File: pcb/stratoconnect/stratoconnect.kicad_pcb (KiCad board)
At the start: 2 copper layers, 61.8 x 40 mm, 37 parts, among them J1 Conn_Coaxial, J2 Conn_02x03_Odd_Even, J3 Conn_01x05_Male, J4 Conn_01x02_Male, J5 Conn_01x03_Male, SW1 SW_SPST, SW2 SW_SPST, U1 RF4463f30, U2 ATmega328PB-A, U3 TPS61022RWU, Y1 CSTNE16M0V530000R0

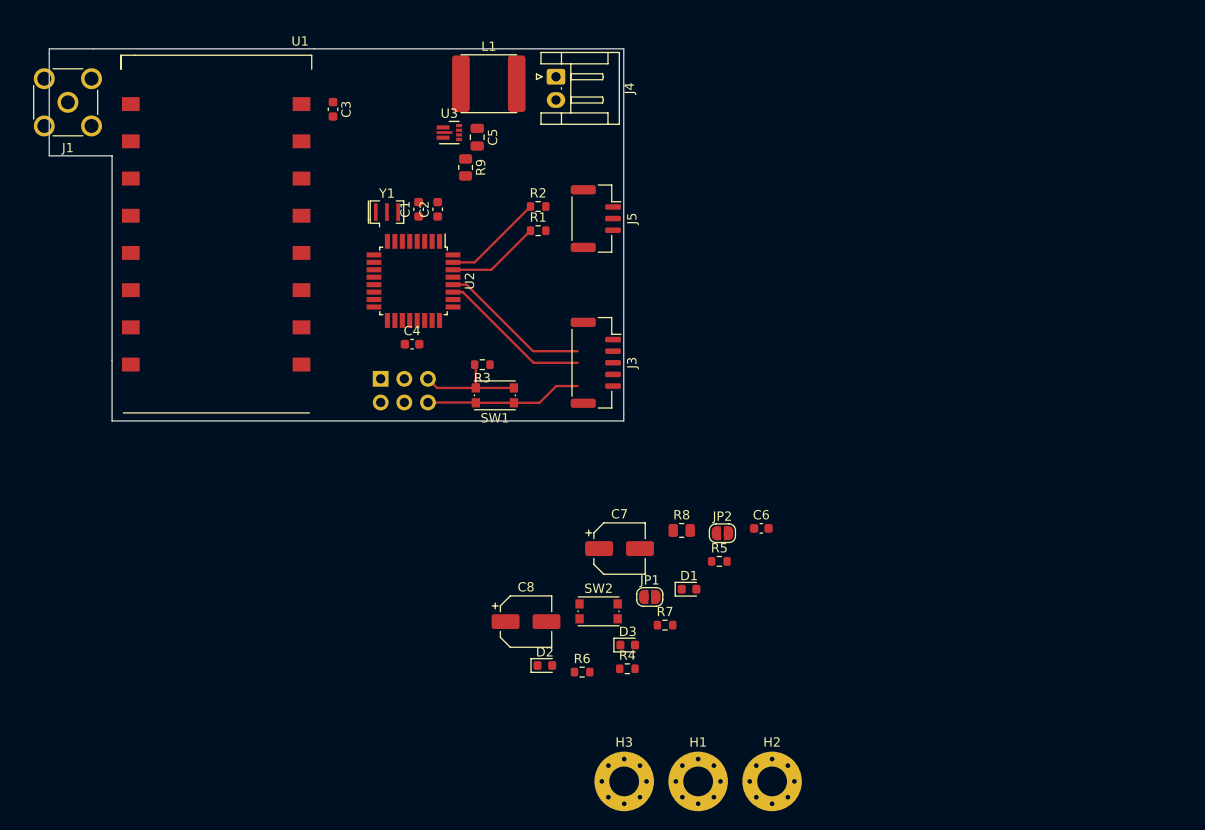
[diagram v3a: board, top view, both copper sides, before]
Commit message: finish routing the smps, need to extend the footprint pads for the rf module
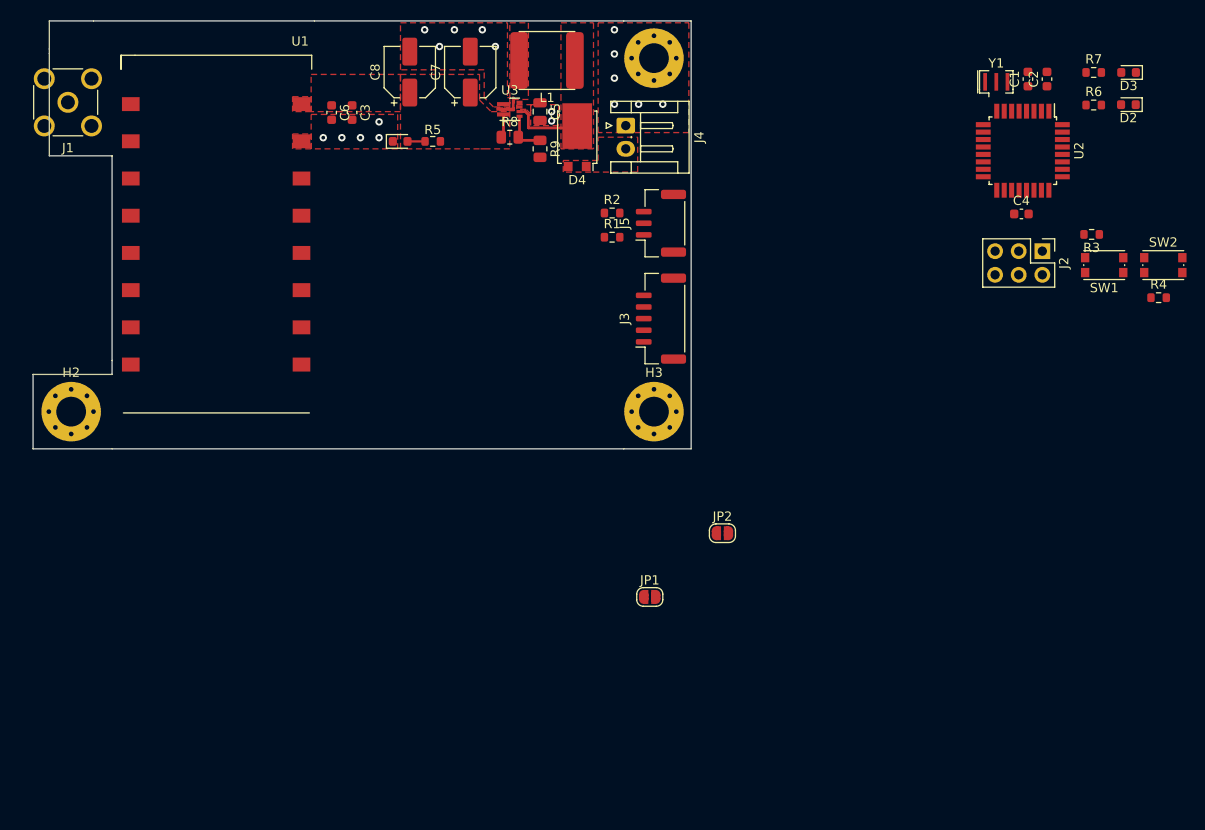
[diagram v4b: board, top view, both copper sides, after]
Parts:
- added D4: ST12199STR, Kevin_Lutzer_Lbr:Diode-TO-277B, F.Cu at (196.0, 59.8)
- J2: moved to F.Cu
- moved D2 87.0 mm to (255.2, 56.2), turned to 180 degrees
- moved H2 85.2 mm to (141.6, 89.2)
- moved R6 82.1 mm to (251.5, 56.3)
- moved D3 81.8 mm to (255.3, 52.8), turned to 180 degrees
- moved H1 77.9 mm to (204.2, 51.2)
- moved R7 75.2 mm to (251.5, 52.8)
- moved J2 72.4 mm to (246.0, 72.0)
- moved SW2 71.2 mm to (259.0, 73.5)
- moved R4 69.7 mm to (258.5, 77.0)
- moved C1 67.0 mm to (244.4, 53.5)
- moved C2 67.0 mm to (246.5, 53.5)
- moved C4 67.0 mm to (243.8, 68.0)
- moved R3 67.0 mm to (251.3, 70.2)
- moved SW1 67.0 mm to (252.7, 73.5)
- moved U2 67.0 mm to (243.9, 61.2)
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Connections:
- C5 pad 1: VDC -> /VDC_FWD
- J4 pad 1: +5V -> GND
- J4 pad 2: GND -> VDC
- L1 pad 1: VDC -> /VDC_FWD
- U3 pad 1: Net-(R8-Pad2) -> +5V
- U3 pad 2: VDC -> /SW
- U3 pad 6: Net-(L1-Pad2) -> /VDC_FWD
- U3 pad 7: +5V -> Net-(R8-Pad2)
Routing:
- net GND: track 16.9 -> 0.00 mm, vias 0 -> 18
- net /SDA: track 16.5 -> 0.00 mm
- net /SCL: track 16.4 -> 0.00 mm
- net /~{RST}: track 12.2 -> 0.00 mm
- net Net-(R2-Pad1): track 10.8 -> 0.00 mm
- net Net-(R1-Pad1): track 10.1 -> 0.00 mm
- net /VDC_FWD: track 0.00 -> 7.84 mm
- net Net-(R8-Pad2): track 0.00 -> 4.78 mm
- net +5V: track 0.00 -> 2.55 mm
- net /SW: track 0.00 -> 2.07 mm
- net Net-(D1-Pad2): track 0.00 -> 1.89 mm
- added copper zone on F.Cu, net +5V
- added copper zone on F.Cu, net /SW
- added copper zone on F.Cu, net /VDC_FWD
- added copper zone on F.Cu, net GND
- added copper zone on F.Cu, net VDC
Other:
- board size 61.8 x 40 mm -> 70.8 x 46 mm
- board text added: "Routed on 0,01mm Placed on 0.25mm"

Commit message: WIP
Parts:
- added R10: 22k, Resistor_SMD:R_0603_1608Metric, F.Cu at (242.2, 85.2)
- added R11: 22k, Resistor_SMD:R_0603_1608Metric, F.Cu at (246.2, 85.2)
- moved C2 65.8 mm to (182.1, 66.9)
- moved C4 65.8 mm to (179.3, 81.4)
- moved D2 65.8 mm to (190.8, 69.7)
- moved D3 65.8 mm to (190.9, 66.2)
- moved J2 65.8 mm to (181.6, 85.4)
- moved R3 65.8 mm to (186.9, 83.6)
- moved R4 65.8 mm to (194.1, 90.4)
- moved R6 65.8 mm to (187.1, 69.7)
- moved R7 65.8 mm to (187.1, 66.2)
- moved SW1 65.8 mm to (188.2, 86.9)
- moved SW2 65.8 mm to (194.6, 86.9)
- moved U2 65.8 mm to (179.5, 74.6)
- moved Y1 65.8 mm to (176.7, 67.2)
- moved C1 65.8 mm to (180.1, 66.9)

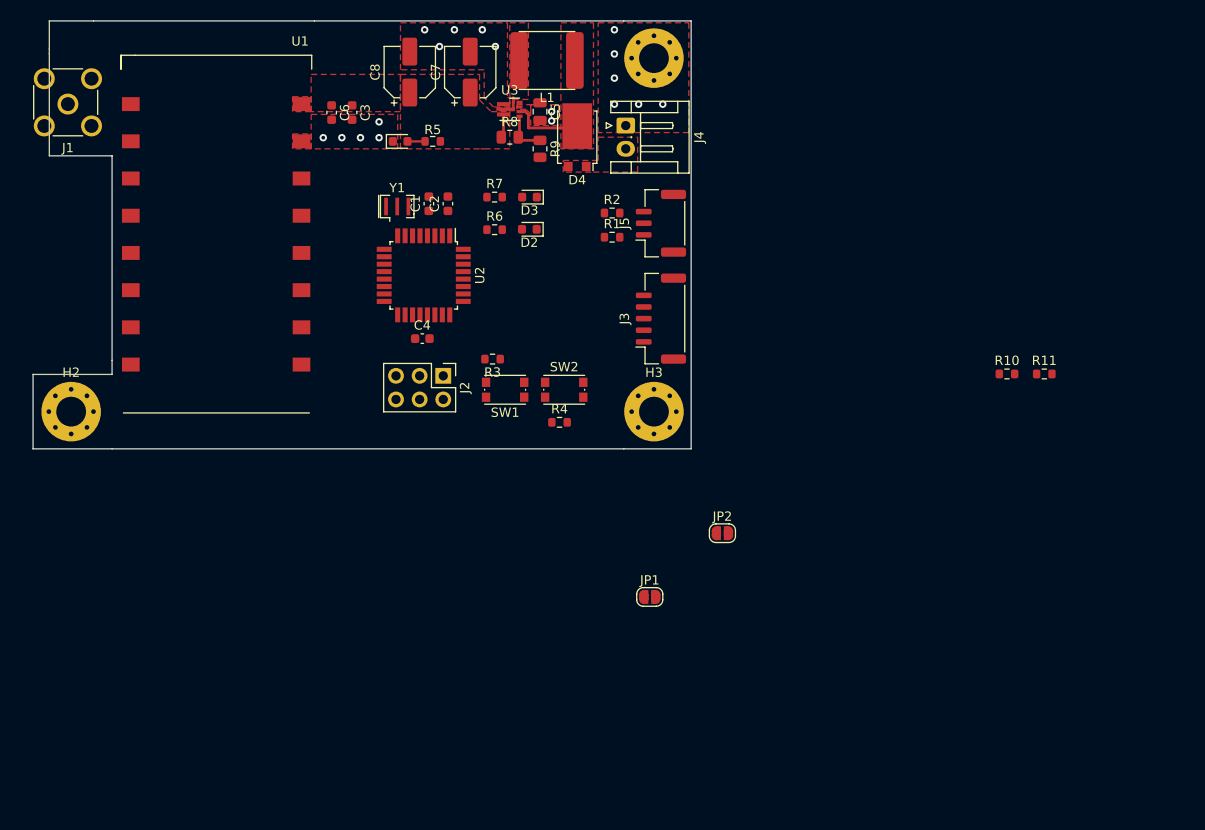
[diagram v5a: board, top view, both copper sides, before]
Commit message: add some of the header labels we need. Finish routing everything but uart, the iscp header, and some other small stuff
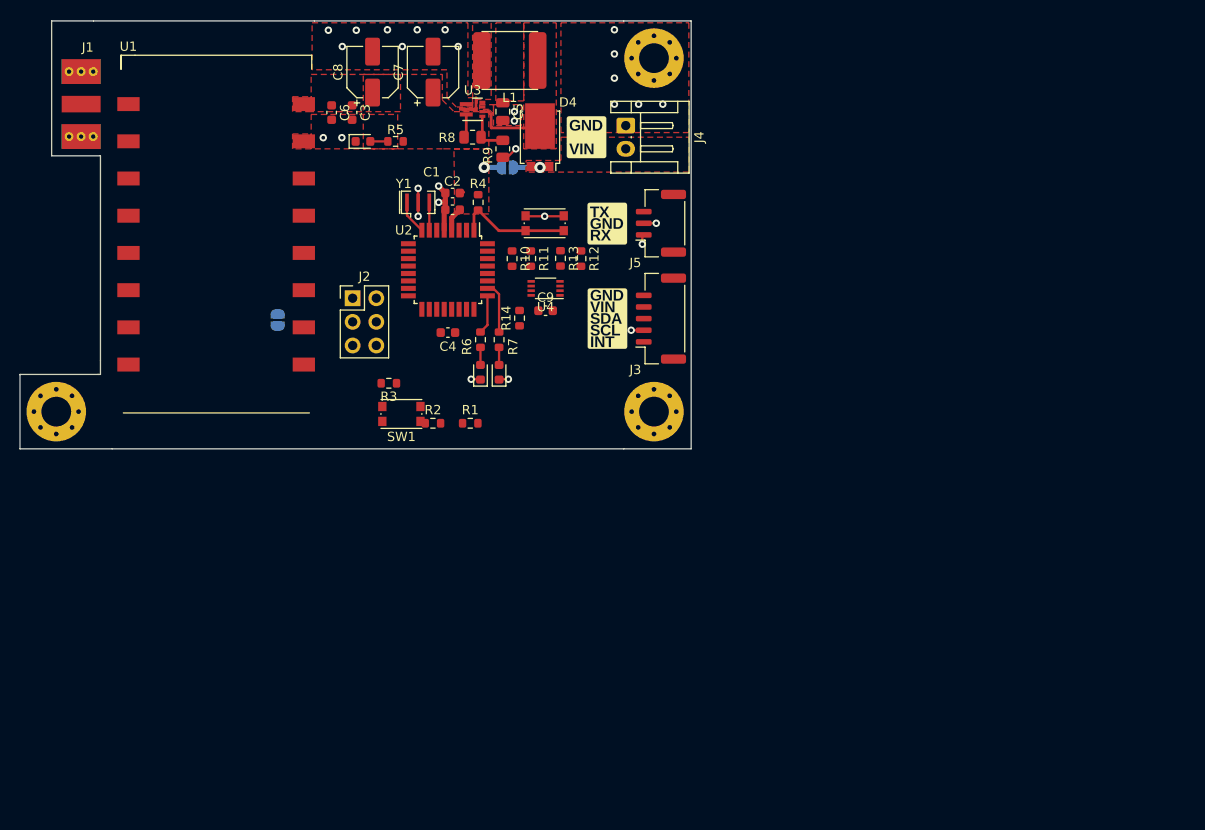
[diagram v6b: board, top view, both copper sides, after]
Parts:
- added C9: 100nF, Capacitor_SMD:C_0603_1608Metric, F.Cu at (192.6, 78.4)
- added R12: 22k, Resistor_SMD:R_0603_1608Metric, F.Cu at (196.4, 72.8)
- added R13: 22k, Resistor_SMD:R_0603_1608Metric, F.Cu at (194.2, 72.8)
- added R14: 10k, Resistor_SMD:R_0603_1608Metric, F.Cu at (189.8, 79.2)
- added U4: PCA9306DC, Package_SO:VSSOP-8_2.3x2mm_P0.5mm, F.Cu at (192.6, 76.0)
- J1: footprint Connector_Coaxial:SMA_Molex_73251-2200_Horizontal -> Connector_Coaxial:SMA_Molex_73251-2120_EdgeMount_Horizontal
- JP1, JP2: moved to B.Cu
- moved R11 56.6 mm to (191.0, 72.8), turned to -90 degrees
- moved R10 54.6 mm to (189.0, 72.8), turned to -90 degrees
- moved JP1 49.9 mm to (163.8, 79.4), turned to -90 degrees
- moved JP2 45.6 mm to (188.5, 63.0)
- moved R2 29.7 mm to (180.5, 90.5)
- moved R4 25.2 mm to (185.3, 66.8), turned to -90 degrees
- moved R1 25.2 mm to (184.5, 90.5)
- moved D3 19.1 mm to (187.6, 85.0), turned to 90 degrees
- moved SW2 18.0 mm to (192.5, 69.0)
- moved D2 16.2 mm to (185.6, 85.0), turned to 90 degrees
- moved R7 15.3 mm to (187.6, 81.5), turned to -90 degrees
- moved J2 12.8 mm to (171.9, 77.1), turned to 0 degrees
- moved R6 11.9 mm to (185.6, 81.5), turned to -90 degrees
- moved R3 11.4 mm to (175.8, 86.2)
- moved SW1 11.4 mm to (177.1, 89.5)
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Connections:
- net Net-(J1-Pad2) renamed /RF_GND
- J3 pad 2: /SCL -> /SCL_LVL
- J3 pad 3: /SDA -> /SDA_LVL
- J3 pad 4: +5V -> +3V3
- J5 pad 1: /RX -> /UART_TX
- J5 pad 3: /TX -> /UART_RX
- R1 pad 2: /UART_TX -> /UART_RX
- R2 pad 2: /UART_RX -> /UART_TX
- R6 pad 1: /TX_LED -> /LED_TX
- R7 pad 1: /RX_LED -> /LED_RX
- U2 pad 1: /LED_TX -> /TRIG
- U2 pad 10: /~{SDN} -> unconnected-(U2-Pad10)
- U2 pad 11: /~{IRQ} -> unconnected-(U2-Pad11)
- U2 pad 13: /~{SPI_CS} -> /~{SDN}
- U2 pad 14: unconnected-(U2-Pad14) -> /~{SPI_CS}
- U2 pad 15: unconnected-(U2-Pad15) -> /SPI_MOSI
- U2 pad 16: unconnected-(U2-Pad16) -> /SPI_MISO
- U2 pad 17: unconnected-(U2-Pad17) -> /SPI_SCK
- U2 pad 19: /SPI_SCK -> unconnected-(U2-Pad19)
- U2 pad 2: /LED_RX -> unconnected-(U2-Pad2)
- U2 pad 25: unconnected-(U2-Pad25) -> /LED_TX
- U2 pad 26: unconnected-(U2-Pad26) -> /LED_RX
- U2 pad 3: /SPI_MOSI -> unconnected-(U2-Pad3)
- U2 pad 32: unconnected-(U2-Pad32) -> /~{IRQ}
- U2 pad 6: /SPI_MISO -> unconnected-(U2-Pad6)
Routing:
- net GND: track 0.00 -> 18.3 mm, vias 18 -> 27
- net /TRIG: track 0.00 -> 12.5 mm
- net /LED_RX: track 0.00 -> 5.57 mm
- net +5V: track 2.55 -> 7.31 mm, vias 0 -> 1
- net /LED_TX: track 0.00 -> 4.20 mm
- net Net-(U2-Pad8): track 0.00 -> 3.66 mm
- net Net-(U2-Pad7): track 0.00 -> 3.00 mm
- net VDC: track 0.00 -> 2.85 mm, vias 0 -> 1
- net Net-(D3-Pad2): track 0.00 -> 2.14 mm
- net Net-(D2-Pad2): track 0.00 -> 2.12 mm
- net /SCL_LVL: track 0.00 -> 1.35 mm, vias 0 -> 1
- net /UART_TX: track 0.00 -> 1.06 mm, vias 0 -> 1
- added copper zone on In1.Cu, net /RF_GND
- added copper zone on In2.Cu, net /RF_GND
- added copper zone on In1.Cu, net GND
- added copper zone on In2.Cu, net GND
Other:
- board size 70.8 x 46 mm -> 72.2 x 46 mm
- copper layers 2 -> 4

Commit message: finish the design
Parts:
- added C10: 100nF, Capacitor_SMD:C_0603_1608Metric, F.Cu at (182.1, 82.8)
- added JP3: SolderJumper_2_Open, Jumper:SolderJumper-2_P1.3mm_Open_RoundedPad1.0x1.5mm, B.Cu at (192.5, 76.0)
- added JP4: SolderJumper_2_Open, Jumper:SolderJumper-2_P1.3mm_Open_RoundedPad1.0x1.5mm, B.Cu at (192.5, 73.5)
- added REF**: OSHW-Logo2_7.3x6mm_SilkScreen, Symbol:OSHW-Logo2_7.3x6mm_SilkScreen, F.Cu at (172.6, 67.4)
- JP1: value SolderJumper_2_Open -> SolderJumper_2_Bridged; footprint Jumper:SolderJumper-2_P1.3mm_Open_RoundedPad1.0x1.5mm -> Jumper:SolderJumper-2_P1.3mm_Bridged_RoundedPad1.0x1.5mm
- moved R2 23.9 mm to (189.8, 68.5)
- moved R1 20.9 mm to (189.8, 70.2)
- moved SW1 4.46 mm to (172.8, 88.5)
- moved SW2 3.58 mm to (194.0, 65.8)
- moved J2 1.55 mm to (171.2, 78.5)
- moved R3 1.37 mm to (177.0, 86.8), turned to -90 degrees
- moved C3 0.30 mm to (171.5, 57.1)
- moved C8 0.25 mm to (174.2, 52.8)
- moved R13 0.20 mm to (194.0, 72.8)
- moved R12 0.15 mm to (196.2, 72.8)
- moved C6 0.10 mm to (169.5, 57.1)
- moved U4 0.10 mm to (192.5, 76.0)
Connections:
- R13 pad 2: /SCL_LVL -> /SDA_LVL
- U2 pad 24: unconnected-(U2-Pad24) -> /~{INT}
- U4 pad 4: /SCL_LVL -> /SDA_LVL
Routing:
- net /SPI_SCK: track 0.00 -> 46.3 mm, vias 0 -> 2
- net /SPI_MOSI: track 0.00 -> 36.9 mm, vias 0 -> 2
- net /SPI_MISO: track 0.00 -> 32.5 mm, vias 0 -> 1
- net /~{RST}: track 0.00 -> 32.4 mm, vias 0 -> 2
- net +5V: track 7.31 -> 34.8 mm, vias 1 -> 8
- net +3V3: track 0.00 -> 20.6 mm, vias 0 -> 2
- net /~{INT}: track 0.00 -> 20.1 mm, vias 0 -> 2
- net /SCL_LVL: track 1.35 -> 18.3 mm
- net /SDA_LVL: track 0.00 -> 15.9 mm, vias 0 -> 1
- net /~{SPI_CS}: track 0.00 -> 15.5 mm, vias 0 -> 1
- net /UART_RX: track 0.00 -> 13.6 mm
- net /UART_TX: track 1.06 -> 13.3 mm, vias 1 -> 2
- net /~{SDN}: track 0.00 -> 12.2 mm
- net GND: track 18.3 -> 29.9 mm, vias 27 -> 36
- net /SDA: track 0.00 -> 7.61 mm, vias 0 -> 3
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- added copper zone on B.Cu, net +5V
- added copper zone on B.Cu, net /RF_GND
- added copper zone on F.Cu, net /RF_GND
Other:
- outline, holes or cut-outs redrawn
- board text added: "For JLCPCB 7628 Coplanar Trace 0.5 mm for spacing 0.397 mm for trace width"

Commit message: add gerbers
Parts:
- C8: value 50uF -> 47uF
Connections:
- R6 pad 1: /LED_TX -> /LED_RX
- R7 pad 1: /LED_RX -> /LED_TX
- U2 pad 25: /LED_TX -> /LED_RX
- U2 pad 26: /LED_RX -> /LED_TX
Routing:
- net /LED_TX: track 4.20 -> 5.57 mm
- net /LED_RX: track 5.57 -> 4.20 mm
- net GND: vias 36 -> 40
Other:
- outline, holes or cut-outs redrawn
